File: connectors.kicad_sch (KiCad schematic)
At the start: 10 parts, among them J1 156-4218-E, J2 USB_C_Receptacle_USB2.0_16P, J3 Conn_01x02_Pin, J4 Conn_01x02_Pin

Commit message: Resnap text to grid + add .gitignore
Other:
- company: (none) -> Tachyon PCBAs
- title: (none) -> Connectors
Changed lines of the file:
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@@
 	(paper "A4")
 	(title_block
-		(date "2024-09-12")
+		(title "Connectors")
+		(date "2024-09-15")
+		(rev "1")
+		(company "Tachyon PCBAs")
+		(comment 1 "first try surely")
+		(comment 2 "USB, S/PDIF Coax, Analog in")
 	)
 	(junction
@@
 	(text "USB C Port"
 		(exclude_from_sim no)
-		(at 75.946 69.088 0)
+		(at 76.835 69.215 0)
 		(effects
 			(font
@@
 	(text "S/PDIF is 75Ω-terminated"
 		(exclude_from_sim no)
-		(at 171.958 73.66 0)
+		(at 172.085 73.66 0)
 		(effects
 			(font
@@
 	(text "Shown are off-board leads"
 		(exclude_from_sim no)
-		(at 198.374 145.542 0)
+		(at 198.12 145.415 0)
 		(effects
 			(font
@@
 	(text "Microphone inputs"
 		(exclude_from_sim no)
-		(at 141.986 105.918 0)
+		(at 142.875 106.045 0)
 		(effects
 			(font
@@
 	(text "S/PDIF I/O (RCA plugs)"
 		(exclude_from_sim no)
-		(at 142.24 56.388 0)
+		(at 142.875 56.515 0)
 		(effects
 			(font
@@
 	(text "5.1kΩ on CC for allowing pulling power from VBUS"
 		(exclude_from_sim no)
-		(at 75.692 131.318 0)
+		(at 75.565 131.445 0)
 		(effects
 			(font

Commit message: Started defining components
Man going down the capacitor dielectric rabbit hole eats up SO MUCH TIME
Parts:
- added D2, D3, D6, D7: PESD3V3Y1BSF, Diode_SMD:Nexperia_DSN0603-2_0.6x0.3mm_P0.4mm, symbol Device:D_TVS
- added D8: PESD5V5C1BL, Diode_SMD:D_SOD-882, symbol Device:D_TVS
- J1: Mouser Part Number (none) -> 156-4218-E
- J2: value USB_C_Receptacle_USB2.0_16P -> USB4105-GF-A-120; Mouser Part Number (none) -> 640-USB4105-GF-A-120
- R11, R12, R3, R9: footprint (none) -> Resistor_SMD:R_0603_1608Metric_Pad0.98x0.95mm_HandSolder
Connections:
- net D+: now also D2.2 (A2)
- net D-: now also D3.2 (A2)
- net DIN_R: now also D7.2 (A2)
- net DOUT_R: now also D6.2 (A2)
- net GND: now also D2.1 (A1), D3.1 (A1), D6.1 (A1), D7.1 (A1), D8.1 (A1)
- net VBUS: now also D8.2 (A2)
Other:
- note added: "Low C TVS for ESD protection"
- moved on the sheet: J1A, J2, R11, R12, R3

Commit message: Fully define components
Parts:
- R11, R12: Mouser Part Number (none) -> 603-RC0603FR-105K1L
- R3, R9: Mouser Part Number (none) -> 603-RT0603FRE0775RL
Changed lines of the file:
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@@
 			)
 		)
-		(property "Datasheet" "~"
+		(property "Datasheet" "https://www.mouser.com/datasheet/2/447/PYu_RC_Group_51_RoHS_L_11-1984063.pdf"
 			(at 104.14 87.63 0)
 			(effects
@@
 			)
 		)
+		(property "Mouser Part Number" "603-RC0603FR-105K1L"
+			(at 104.14 87.63 0)
+			(effects
+				(font
+					(size 1.27 1.27)
+				)
+				(hide yes)
+			)
+		)
 		(pin "2"
 		)
@@
 			)
 		)
-		(property "Datasheet" "~"
+		(property "Datasheet" "https://www.mouser.com/datasheet/2/447/PYu_RC_Group_51_RoHS_L_11-1984063.pdf"
 			(at 104.14 85.09 0)
 			(effects
@@
 		)
 		(property "Description" "Resistor"
+			(at 104.14 85.09 0)
+			(effects
+				(font
+					(size 1.27 1.27)
+				)
+				(hide yes)
+			)
+		)
+		(property "Mouser Part Number" "603-RC0603FR-105K1L"
 			(at 104.14 85.09 0)
 			(effects
@@
 			)
 		)
-		(property "Datasheet" "~"
+		(property "Datasheet" "https://www.mouser.com/datasheet/2/447/PYu_RT_1_to_0_01_RoHS_L_15-3461507.pdf"
 			(at 186.69 82.55 0)
 			(effects
@@
 		)
 		(property "Description" "Resistor"
+			(at 186.69 82.55 0)
+			(effects
+				(font
+					(size 1.27 1.27)
+				)
+				(hide yes)
+			)
+		)
+		(property "Mouser Part Number" "603-RT0603FRE0775RL"
 			(at 186.69 82.55 0)
 			(effects
@@
 			)
 		)
-		(property "Datasheet" "~"
+		(property "Datasheet" "https://www.mouser.com/datasheet/2/447/PYu_RT_1_to_0_01_RoHS_L_15-3461507.pdf"
 			(at 186.69 60.96 0)
 			(effects
@@
 			(at 186.69 60.96 0)
 			(effects
+				(font
+					(size 1.27 1.27)
+				)
+				(hide yes)
+			)
+		)
+		(property "Mouser Part Number" "603-RT0603FRE0775RL"
+			(at 186.69 60.96 0)
+			(effects

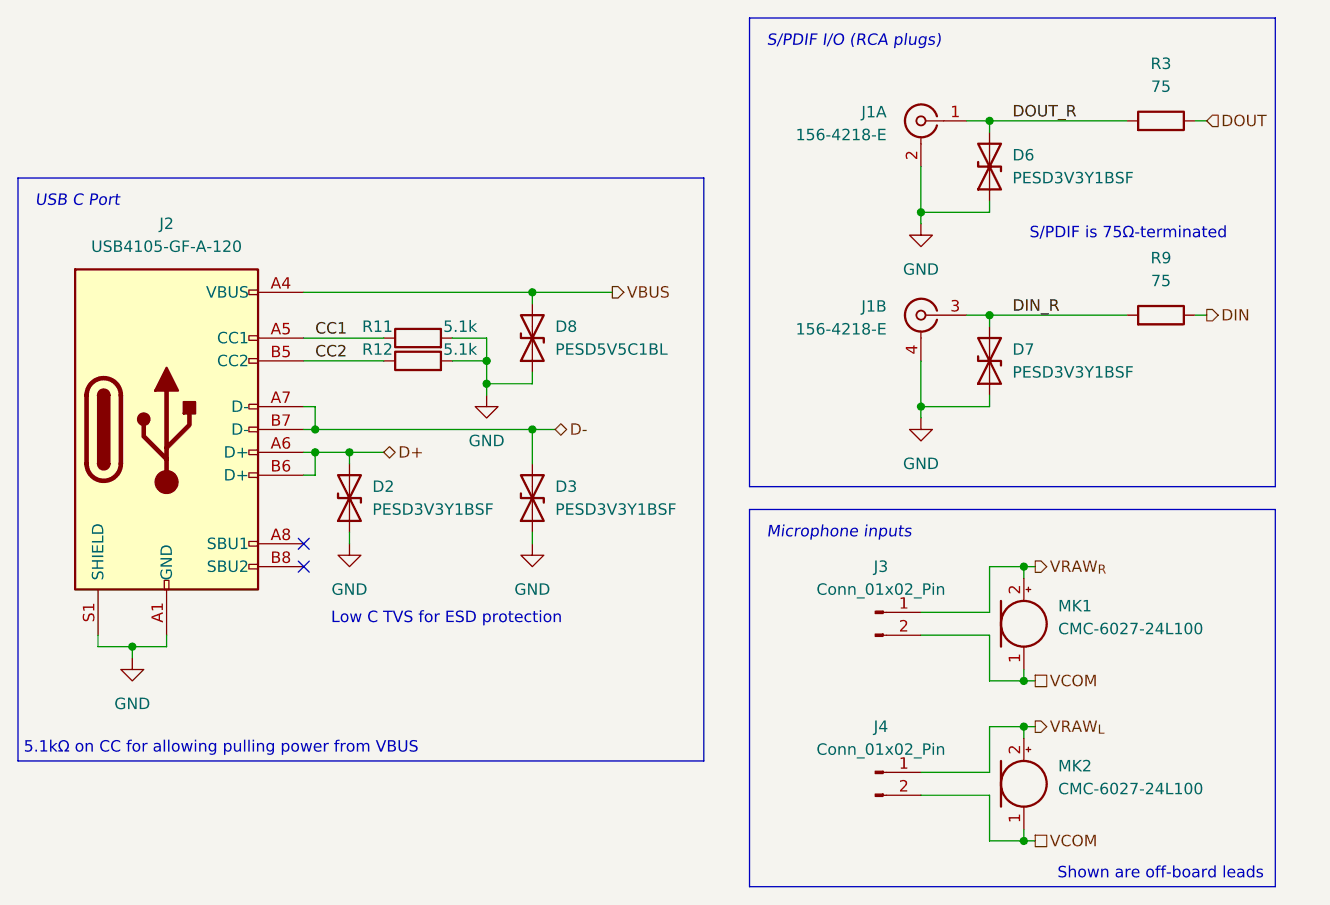
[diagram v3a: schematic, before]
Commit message: Replace S/PIDF RCA jack with a singular one since I won't need an input one
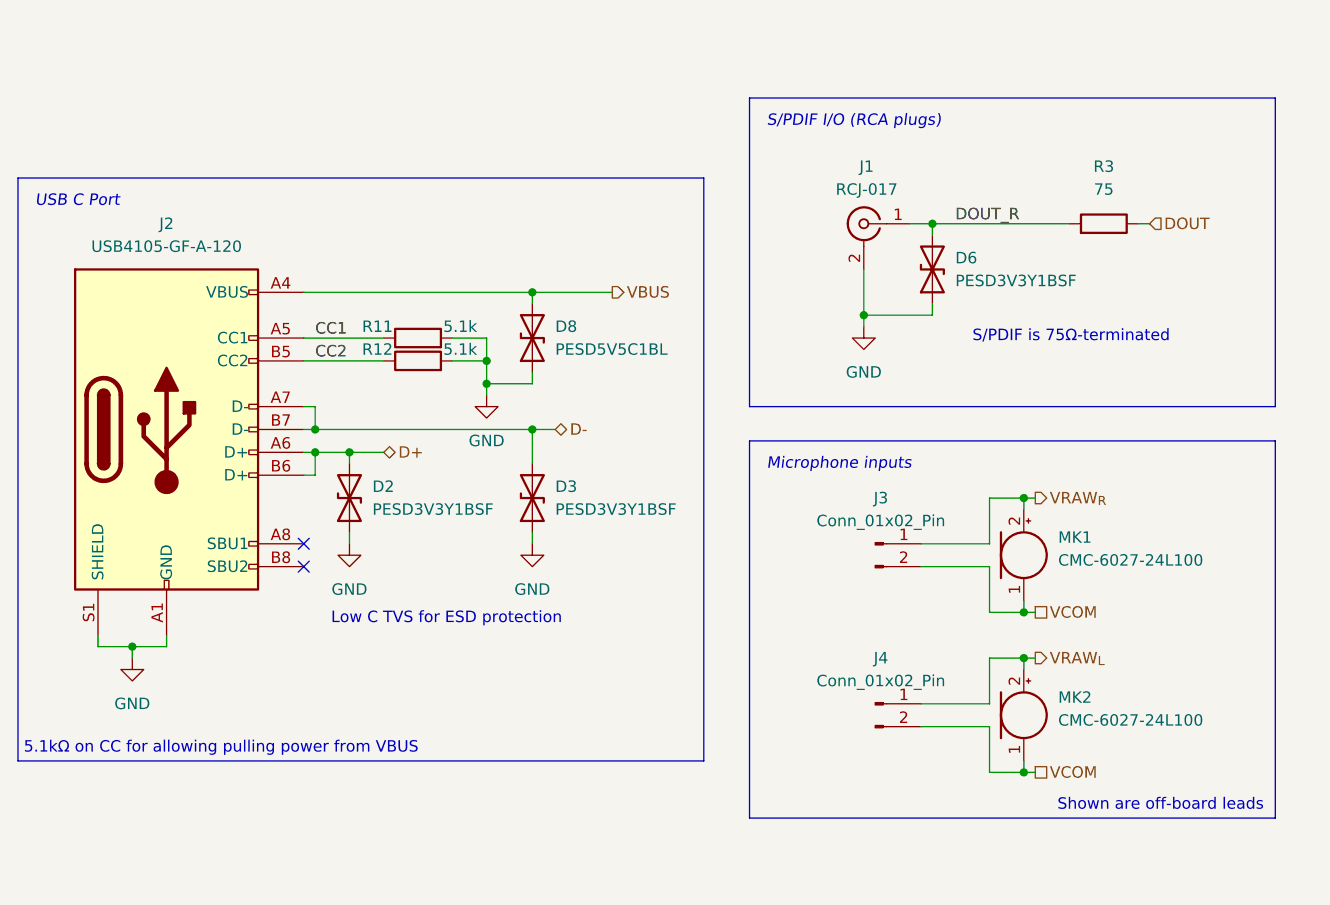
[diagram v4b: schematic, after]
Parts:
- removed D7: PESD3V3Y1BSF, Diode_SMD:Nexperia_DSN0603-2_0.6x0.3mm_P0.4mm, symbol Device:D_TVS
- removed unit 2 of J1
- removed R9: 75, Resistor_SMD:R_0603_1608Metric_Pad0.98x0.95mm_HandSolder, symbol Device:R
- J1: value 156-4218-E -> RCJ-017; footprint binauralmic:1564218E -> binauralmic:RCJ014; symbol Connector:Conn_Coaxial_x2_Isolated -> Connector:Conn_Coaxial; Mouser Part Number 156-4218-E -> 490-RCJ-017
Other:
- moved on the sheet: D6, J1, J3, J4, MK1, MK2, R3

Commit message: Add analog volume control
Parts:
- D2, D3, D6: Mouser Part Number (none) -> 771-PESD3V3Y1BSFYL
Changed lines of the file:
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@@
+			)
+		)
+		(property "Mouser Part Number" "771-PESD3V3Y1BSFYL"
+			(at 116.84 102.87 0)
+			(effects
+				(font
+					(size 1.27 1.27)
+				)
+				(hide yes)
 			)
 		)
@@
 			)
 		)
+		(property "Mouser Part Number" "771-PESD3V3Y1BSFYL"
+			(at 96.52 102.87 0)
+			(effects
+				(font
+					(size 1.27 1.27)
+				)
+				(hide yes)
+			)
+		)
 		(pin "2"
 		)
@@
 			(at 161.29 77.47 0)
 			(effects
+				(font
+					(size 1.27 1.27)
+				)
+				(hide yes)
+			)
+		)
+		(property "Mouser Part Number" "771-PESD3V3Y1BSFYL"
+			(at 161.29 77.47 0)
+			(effects

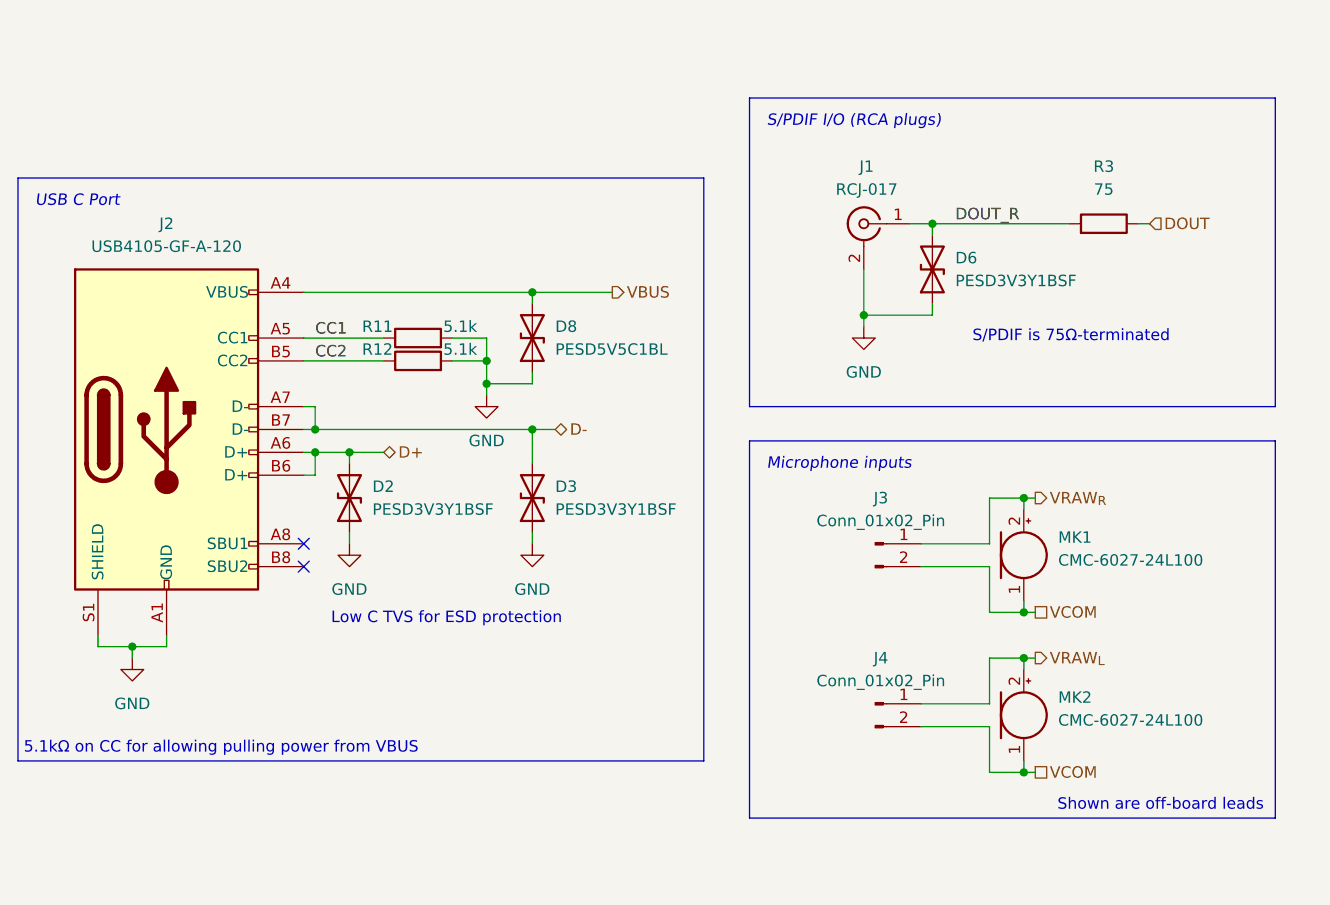
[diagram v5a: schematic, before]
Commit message: Remove potentiometer
Will have to find a different solution for volume control
Just do it OS-side?
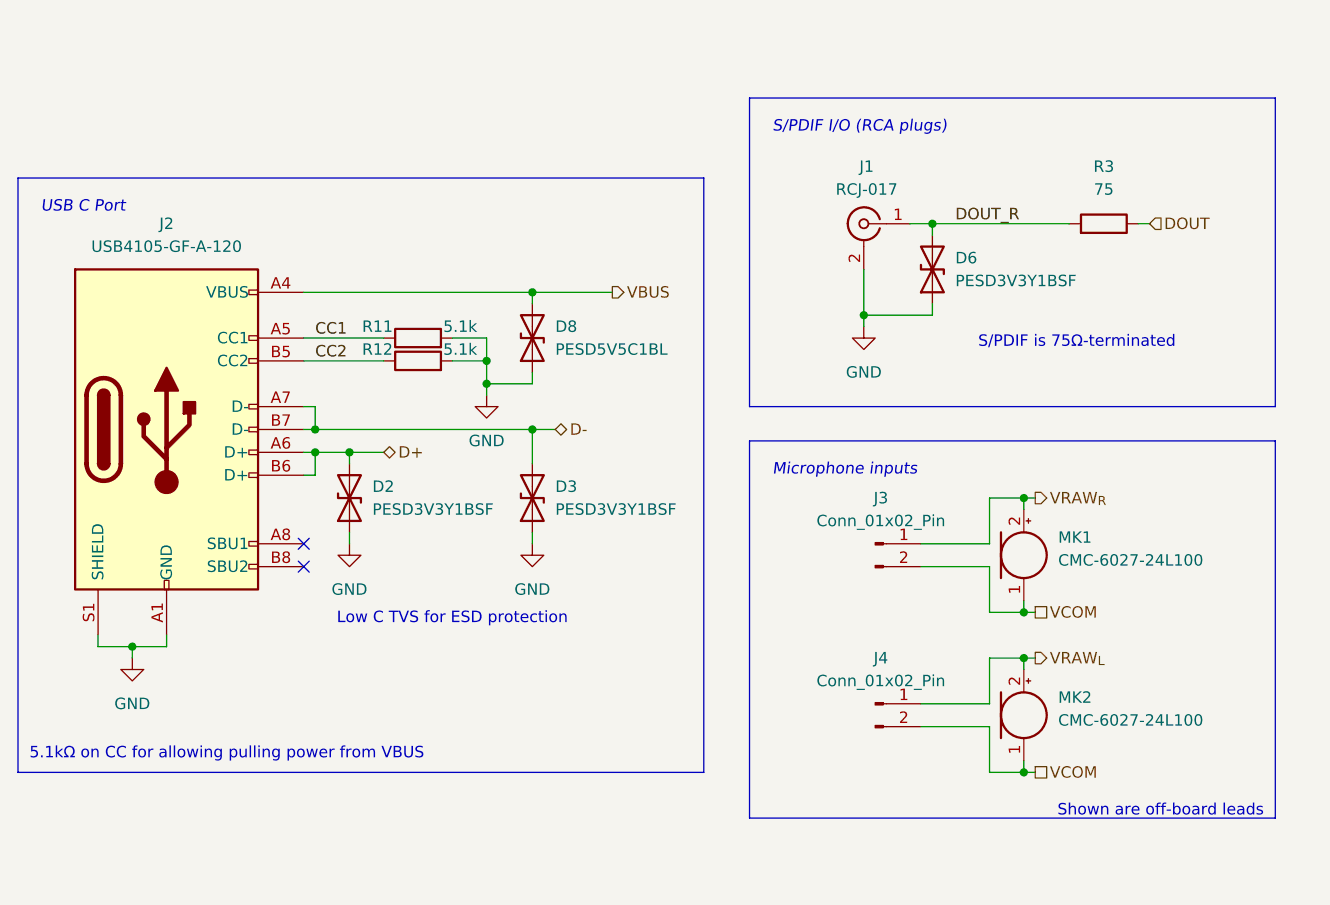
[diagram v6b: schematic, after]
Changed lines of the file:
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@@
 	(rectangle
 		(start 59.69 67.31)
-		(end 135.89 132.08)
+		(end 135.89 133.35)
 		(stroke
 			(width 0)
@@
 	(text "USB C Port"
 		(exclude_from_sim no)
-		(at 61.595 69.215 0)
+		(at 62.23 69.85 0)
 		(effects
 			(font
@@
 	(text "S/PDIF is 75Ω-terminated"
 		(exclude_from_sim no)
-		(at 165.735 85.725 0)
+		(at 166.37 86.36 0)
 		(effects
 			(font
@@
 	(text "Shown are off-board leads"
 		(exclude_from_sim no)
-		(at 198.12 137.795 0)
+		(at 198.12 138.43 0)
 		(effects
 			(font
@@
 	(text "Microphone inputs"
 		(exclude_from_sim no)
-		(at 142.875 98.425 0)
+		(at 143.51 99.06 0)
 		(effects
 			(font
@@
 	(text "S/PDIF I/O (RCA plugs)"
 		(exclude_from_sim no)
-		(at 142.875 60.325 0)
+		(at 143.51 60.96 0)
 		(effects
 			(font
@@
 	(text "5.1kΩ on CC for allowing pulling power from VBUS"
 		(exclude_from_sim no)
-		(at 60.325 131.445 0)
+		(at 60.96 132.08 0)
 		(effects
 			(font
@@
 	(text "Low C TVS for ESD protection"
 		(exclude_from_sim no)
-		(at 107.315 115.57 0)
+		(at 107.95 115.57 0)
 		(effects
 			(font

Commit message: Starting layout
Also why are the mf diodes so small
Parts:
- D1: renamed from D6; footprint Diode_SMD:Nexperia_DSN0603-2_0.6x0.3mm_P0.4mm -> Diode_SMD:D_0201_0603Metric_Pad0.64x0.40mm_HandSolder
- D3: renamed from D2; footprint Diode_SMD:Nexperia_DSN0603-2_0.6x0.3mm_P0.4mm -> Diode_SMD:D_0201_0603Metric_Pad0.64x0.40mm_HandSolder
- D4: renamed from D3; footprint Diode_SMD:Nexperia_DSN0603-2_0.6x0.3mm_P0.4mm -> Diode_SMD:D_0201_0603Metric_Pad0.64x0.40mm_HandSolder
- renumbered D8 to D2, R3 to R1, R11 to R2, R12 to R3
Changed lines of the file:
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@@
 		(dnp no)
 		(fields_autoplaced yes)
-		(property "Reference" "#PWR020"
+		(property "Reference" "#PWR05"
 			(at 111.76 97.79 0)
 			(effects
@@
 			(project "BinauralMic"
 				(path "/d9e790b9-8aa4-4e58-8bd7-6ef4bc890627/ed99070c-0835-415c-8078-0f260c71dd6d"
-					(reference "#PWR020")
+					(reference "#PWR05")
 					(unit 1)
 				)
@@
 		(dnp no)
 		(fields_autoplaced yes)
-		(property "Reference" "#PWR026"
+		(property "Reference" "#PWR07"
 			(at 116.84 114.3 0)
 			(effects
@@
 			(project "BinauralMic"
 				(path "/d9e790b9-8aa4-4e58-8bd7-6ef4bc890627/ed99070c-0835-415c-8078-0f260c71dd6d"
-					(reference "#PWR026")
+					(reference "#PWR07")
 					(unit 1)
 				)
@@
 		(dnp no)
 		(fields_autoplaced yes)
-		(property "Reference" "D8"
+		(property "Reference" "D2"
 			(at 119.38 83.8199 90)
 			(effects
@@
 			(project "BinauralMic"
 				(path "/d9e790b9-8aa4-4e58-8bd7-6ef4bc890627/ed99070c-0835-415c-8078-0f260c71dd6d"
-					(reference "D8")
+					(reference "D2")
 					(unit 1)
 				)
@@
 		(dnp no)
 		(fields_autoplaced yes)
-		(property "Reference" "#PWR022"
+		(property "Reference" "#PWR06"
 			(at 96.52 114.3 0)
 			(effects
@@
 			(project "BinauralMic"
 				(path "/d9e790b9-8aa4-4e58-8bd7-6ef4bc890627/ed99070c-0835-415c-8078-0f260c71dd6d"
-					(reference "#PWR022")
+					(reference "#PWR06")
 					(unit 1)
 				)
@@
 		(on_board yes)
 		(dnp no)
-		(property "Reference" "R12"
+		(property "Reference" "R3"
 			(at 101.346 86.36 90)
 			(effects
@@
 			(project "BinauralMic"
 				(path "/d9e790b9-8aa4-4e58-8bd7-6ef4bc890627/ed99070c-0835-415c-8078-0f260c71dd6d"
-					(reference "R12")
+					(reference "R3")
 					(unit 1)
 				)
@@
 		(dnp no)
 		(fields_autoplaced yes)
-		(property "Reference" "D3"
+		(property "Reference" "D4"
 			(at 119.38 101.5999 90)
 			(effects
@@
 			)
 		)
-		(property "Footprint" "Diode_SMD:Nexperia_DSN0603-2_0.6x0.3mm_P0.4mm"
+		(property "Footprint" "Diode_SMD:D_0201_0603Metric_Pad0.64x0.40mm_HandSolder"
 			(at 116.84 102.87 0)
 			(effects
@@
 			(project "BinauralMic"
 				(path "/d9e790b9-8aa4-4e58-8bd7-6ef4bc890627/ed99070c-0835-415c-8078-0f260c71dd6d"
-					(reference "D3")
+					(reference "D4")
 					(unit 1)
 				)
@@
 		(on_board yes)
 		(dnp no)
-		(property "Reference" "R11"
+		(property "Reference" "R2"
 			(at 101.346 83.82 90)
 			(effects
@@
 			(project "BinauralMic"
 				(path "/d9e790b9-8aa4-4e58-8bd7-6ef4bc890627/ed99070c-0835-415c-8078-0f260c71dd6d"
-					(reference "R11")
+					(reference "R2")
 					(unit 1)
 				)
@@
 		(dnp no)
 		(fields_autoplaced yes)
-		(property "Reference" "#PWR016"
+		(property "Reference" "#PWR04"
 			(at 153.67 90.17 0)
 			(effects
@@
 			(project "BinauralMic"
 				(path "/d9e790b9-8aa4-4e58-8bd7-6ef4bc890627/ed99070c-0835-415c-8078-0f260c71dd6d"
-					(reference "#PWR016")
+					(reference "#PWR04")
 					(unit 1)
 				)
@@
 		(dnp no)
 		(fields_autoplaced yes)
-		(property "Reference" "D2"
+		(property "Reference" "D3"
 			(at 99.06 101.5999 90)
 			(effects
@@
 			)
 		)
-		(property "Footprint" "Diode_SMD:Nexperia_DSN0603-2_0.6x0.3mm_P0.4mm"
+		(property "Footprint" "Diode_SMD:D_0201_0603Metric_Pad0.64x0.40mm_HandSolder"
 			(at 96.52 102.87 0)
 			(effects
@@
 			(project ""
 				(path "/d9e790b9-8aa4-4e58-8bd7-6ef4bc890627/ed99070c-0835-415c-8078-0f260c71dd6d"
-					(reference "D2")
+					(reference "D3")
 					(unit 1)
 				)
@@
 		(dnp no)
 		(fields_autoplaced yes)
-		(property "Reference" "#PWR021"
+		(property "Reference" "#PWR08"
 			(at 72.39 127 0)
 			(effects
@@
 			(project "BinauralMic"
 				(path "/d9e790b9-8aa4-4e58-8bd7-6ef4bc890627/ed99070c-0835-415c-8078-0f260c71dd6d"
-					(reference "#PWR021")
+					(reference "#PWR08")
 					(unit 1)
 				)
@@
 		(dnp no)
 		(fields_autoplaced yes)
-		(property "Reference" "D6"
+		(property "Reference" "D1"
 			(at 163.83 76.1999 90)
 			(effects
@@
 			)
 		)
-		(property "Footprint" "Diode_SMD:Nexperia_DSN0603-2_0.6x0.3mm_P0.4mm"
+		(property "Footprint" "Diode_SMD:D_0201_0603Metric_Pad0.64x0.40mm_HandSolder"
 			(at 161.29 77.47 0)
 			(effects
@@
 			(project "BinauralMic"
 				(path "/d9e790b9-8aa4-4e58-8bd7-6ef4bc890627/ed99070c-0835-415c-8078-0f260c71dd6d"
-					(reference "D6")
+					(reference "D1")
 					(unit 1)
 				)
@@
 		(dnp no)
 		(fields_autoplaced yes)
-		(property "Reference" "R3"
+		(property "Reference" "R1"
 			(at 180.34 66.04 90)
 			(effects
@@
 			(project "BinauralMic"
 				(path "/d9e790b9-8aa4-4e58-8bd7-6ef4bc890627/ed99070c-0835-415c-8078-0f260c71dd6d"
-					(reference "R3")
-					(unit 1)
-				)
+					(reference "R1")
+					(unit 1)
+				)
